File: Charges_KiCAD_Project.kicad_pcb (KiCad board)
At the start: 4 copper layers, 79.2 x 87.2 mm, 43 parts, among them IC1 TP124005-2, IC2 STM32L562VET6Q, J1 TB002-500-04BE, J2 TB002-500-04BE, J3 L717SDC37P1ACH4F, Q1 SI7232DN-T1-GE3, Q2 SI7232DN-T1-GE3, U1 MS5607-02BA

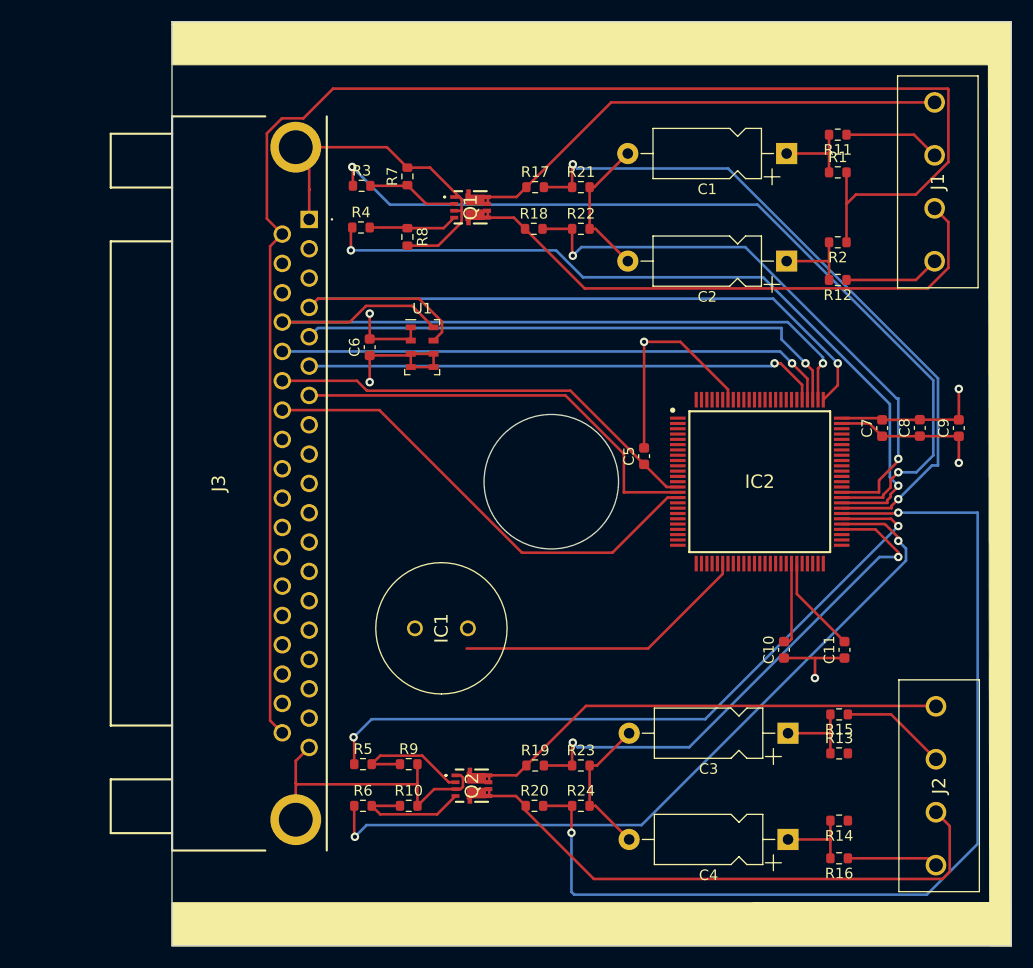
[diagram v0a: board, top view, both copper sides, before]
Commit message: updated traces
trace widths were updated
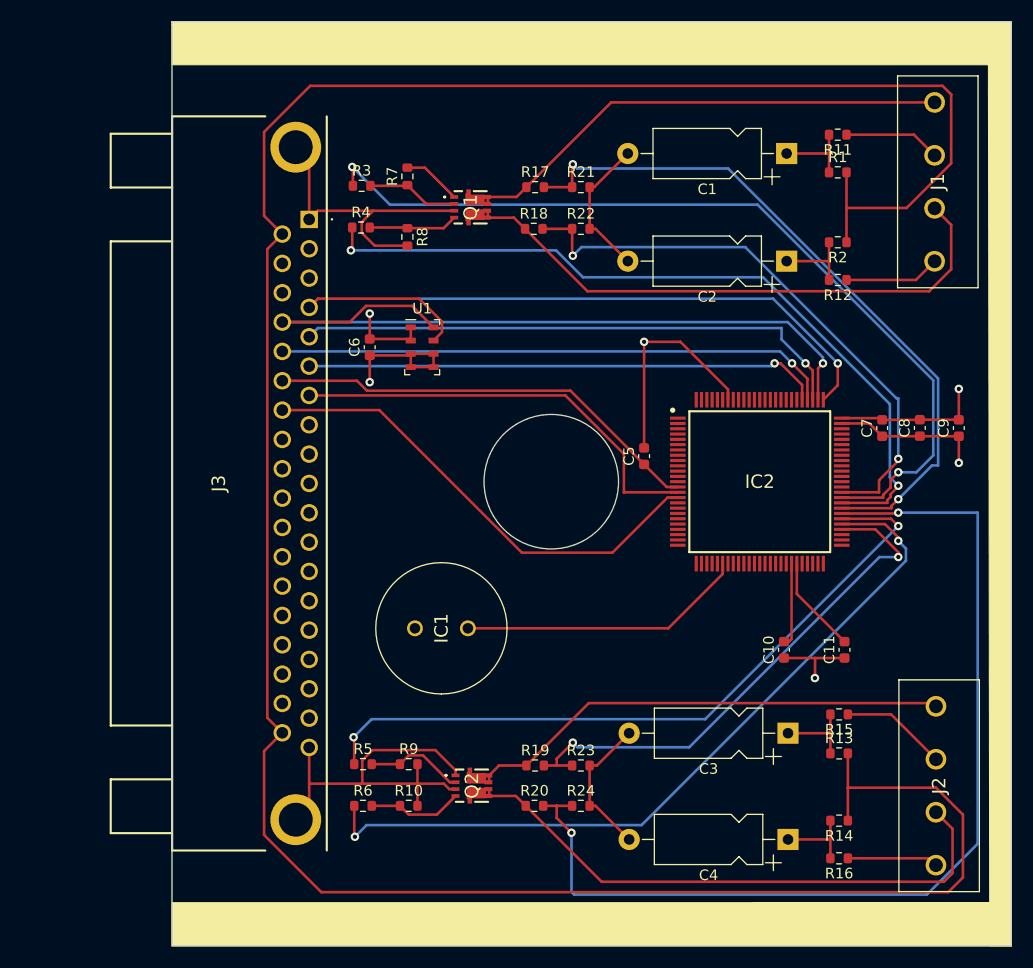
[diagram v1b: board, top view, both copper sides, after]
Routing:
- net +5V: track 149.0 -> 253.7 mm
- net GND: track 149.8 -> 157.6 mm
- net Net-(Q2-Pad4): track 11.6 -> 8.98 mm
- net Net-(Q2-Pad2): track 11.9 -> 9.30 mm
- net /Buzzer_Excitation: track 28.1 -> 27.2 mm
- net /Sense_C: track 49.9 -> 50.6 mm
- net /Fet_B: track 53.9 -> 54.5 mm
- net /Sense_D: track 95.5 -> 96.1 mm
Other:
- net class 1amp added: clearance 0.2, trace_width 0.300387, via_dia 0.8, via_drill 0.4
- net class 5amp added: clearance 0.2, trace_width 2.76552, via_dia 0.8, via_drill 0.4

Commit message: updated pcb
pcb wasnt fully aligned. that is now fixed
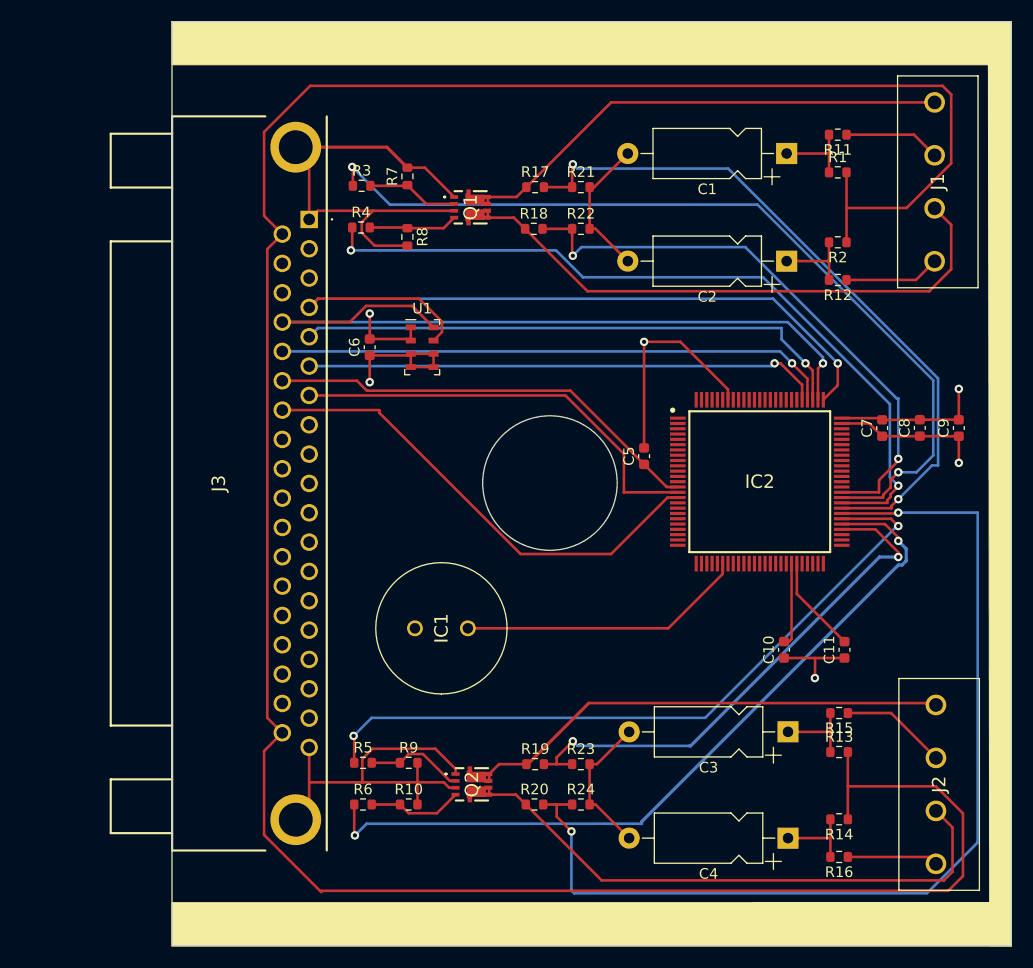
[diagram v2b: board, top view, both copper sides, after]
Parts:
- moved C4 0.13 mm to (155.1, 129.5)
- moved Q2 0.13 mm to (125.2, 124.5)
- moved R10 0.13 mm to (119.3, 126.4)
- moved R20 0.13 mm to (131.1, 126.4)
- moved R24 0.13 mm to (135.5, 126.4)
- moved R5 0.13 mm to (114.9, 122.4)
- moved R6 0.13 mm to (114.9, 126.4)
- moved R9 0.13 mm to (119.3, 122.4)
- moved C3 0.13 mm to (155.1, 119.5)
- moved J2 0.13 mm to (169.0, 117.0)
- moved R13 0.13 mm to (159.9, 121.4)
- moved R14 0.13 mm to (159.9, 127.8)
- moved R15 0.13 mm to (159.9, 117.7)
- moved R19 0.13 mm to (131.2, 122.6)
- moved R23 0.13 mm to (135.5, 122.6)
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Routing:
- net GND: track 157.6 -> 168.9 mm
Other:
- outline, holes or cut-outs redrawn

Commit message: updated board
updated the board again
added a crystal
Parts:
- added Y1: 32mhz, Crystal:Crystal_HC49-4H_Vertical, F.Cu at (151.2, 108.8)
- moved C1 10.1 mm to (146.0, 60.2)
- moved C3 9.41 mm to (146.0, 117.0)
- moved C4 9.39 mm to (146.0, 132.0)
- moved C10 9.30 mm to (145.8, 109.2)
- moved R1 9.06 mm to (152.0, 62.0)
- moved R11 9.04 mm to (152.0, 58.5)
- moved C2 8.94 mm to (146.0, 75.2)
- moved IC1 8.85 mm to (116.0, 110.0)
- moved C9 8.39 mm to (163.0, 92.6), turned to 0 degrees
- moved J3 8.36 mm to (101.5, 71.2)
- moved R14 8.28 mm to (152.0, 130.2)
- moved R15 8.27 mm to (152.0, 115.2)
- moved R16 8.26 mm to (152.0, 133.8)
- moved R13 8.25 mm to (152.0, 119.0)
- moved J2 7.79 mm to (161.2, 117.0)
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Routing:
- net /Sense_D: track 96.0 -> 55.1 mm
- net +5V: track 253.7 -> 222.4 mm
- net GND: track 168.9 -> 182.4 mm, vias 4 -> 3
- net /Fire_A: track 83.0 -> 72.6 mm
- net /Fire: track 40.7 -> 50.8 mm
- net /Sense_A: track 66.8 -> 57.9 mm
- net /SWDIO: track 72.7 -> 64.0 mm, vias 1 -> 0
- net /Fire_Redundant: track 45.3 -> 53.0 mm
- net /NRST: track 41.5 -> 48.7 mm
- net /Buzzer_Excitation: track 27.2 -> 33.3 mm
- net /Alert_sda: track 52.6 -> 58.1 mm, vias 1 -> 0
- net /Alert_Active: track 49.6 -> 54.4 mm, vias 1 -> 0
- net /Fire_B: track 73.7 -> 69.1 mm
- net /Sense_B: track 55.5 -> 51.0 mm
- net /Alert_scl: track 52.9 -> 56.7 mm, vias 1 -> 0
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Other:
- board size 79.2 x 87.2 mm -> 80 x 87.2 mm

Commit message: Changes to PCB
noticed that 3v3 plane only had like 2 connections, so i changed it to a mixed with mainly 5v instead
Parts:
- moved R13 0.50 mm to (152.0, 119.5)
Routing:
- net +5V: track 222.4 -> 22.5 mm, vias 0 -> 2
- net +3V3: track 21.9 -> 153.6 mm
- net GND: track 182.4 -> 186.4 mm
- net /Fet_D: track 54.2 -> 55.6 mm
- net /Fet_B: track 54.2 -> 55.6 mm
- net /Fet_A: track 46.5 -> 47.4 mm
- net /Fet_C: track 46.5 -> 47.4 mm
- added copper zone on power, net +5V
- removed copper zone on 3v3, net +3V3
